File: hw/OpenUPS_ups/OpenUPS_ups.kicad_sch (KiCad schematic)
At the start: 15 parts, among them J101 XT60PW-M, J102 Barrel Jack, J103 Screw Terminal, J104 Screw Terminal, J105 Screw Terminal, J106 JST XH, J107 JST XH, U101 AVR32DB28x-xSO

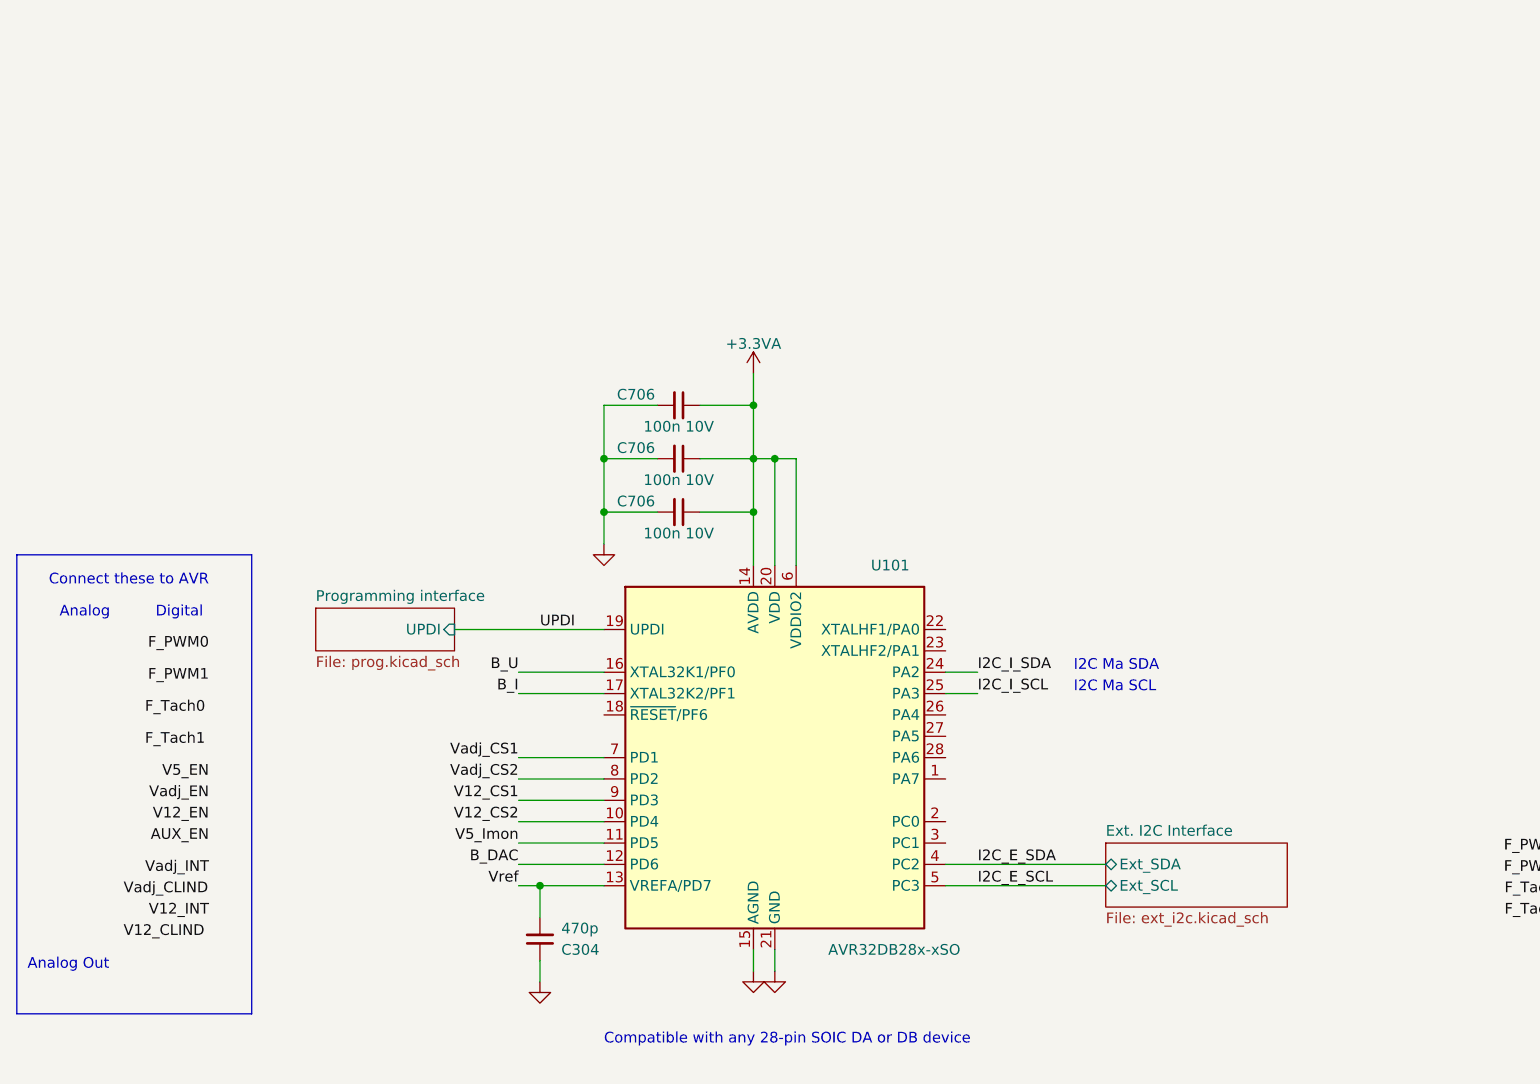
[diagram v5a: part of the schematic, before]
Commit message: Issue #20: replaced AVR with 48-pin TQFP
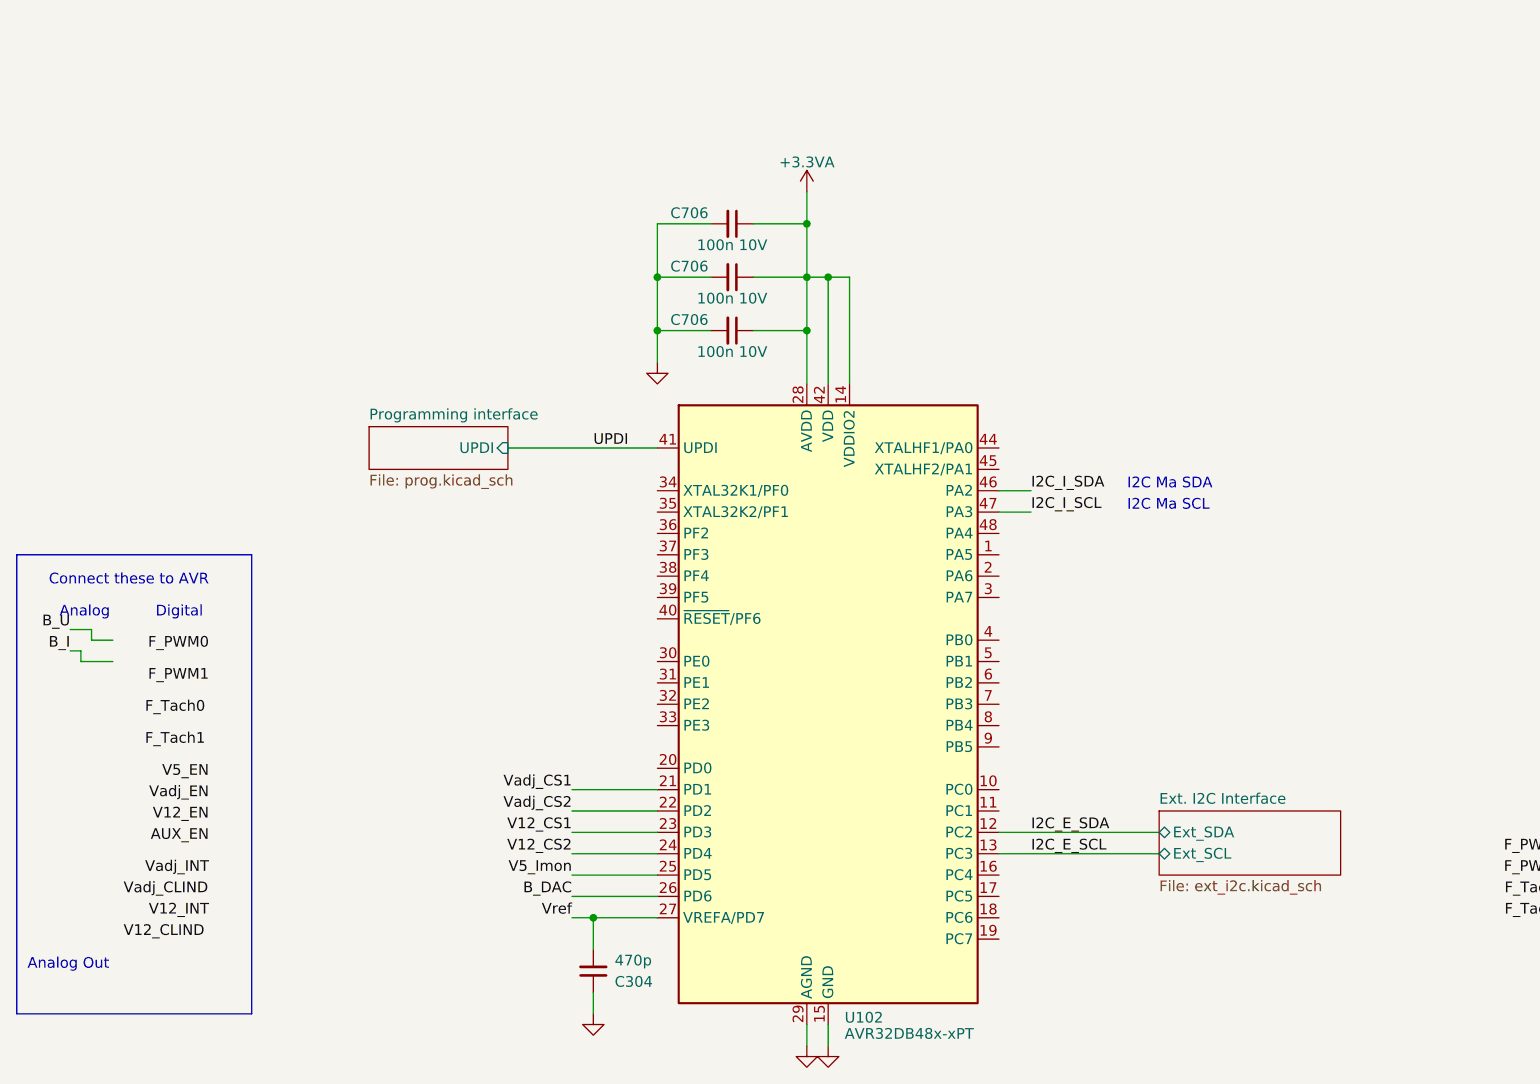
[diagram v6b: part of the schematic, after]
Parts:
- removed U101: AVR32DB28x-xSO, Package_SO:SOIC-28W_7.5x17.9mm_P1.27mm, symbol MCU_Microchip_AVR_Dx:AVR32DB28x-xSO
- added U102: AVR32DB48x-xPT, Package_QFP:TQFP-48_7x7mm_P0.5mm, symbol MCU_Microchip_AVR_Dx:AVR32DB48x-xPT
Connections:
- net +3.3VA: now also U102.14 (VDDIO2), U102.28 (AVDD), U102.42 (VDD)
- net B_DAC: now also U102.26 (PD6)
- net GND: now also U102.15 (GND), U102.29 (AGND), U102.43 (GND)
- net I2C_E_SCL: now also U102.13 (PC3)
- net I2C_E_SDA: now also U102.12 (PC2)
- net I2C_I_SCL: now also U102.47 (PA3)
- net I2C_I_SDA: now also U102.46 (PA2)
- net UPDI: now also U102.41 (UPDI)
- net V12_CS1: now also U102.23 (PD3)
- net V12_CS2: now also U102.24 (PD4)
- net V5_Imon: now also U102.25 (PD5)
- net Vadj_CS1: now also U102.21 (PD1)
- net Vadj_CS2: now also U102.22 (PD2)
- net Vref: now also U102.27 (VREFA/PD7)
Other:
- note removed: "Compatible with any 28-pin SOIC DA or DB device"
- moved on the sheet: C304, C706

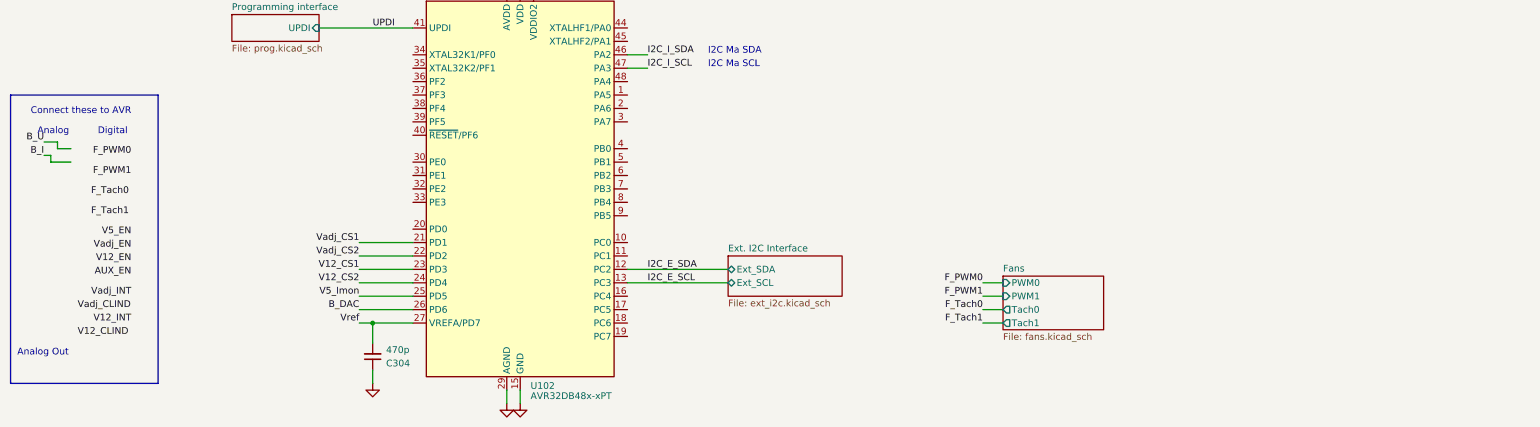
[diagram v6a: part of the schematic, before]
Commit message: Issue #16: Added LED indicators
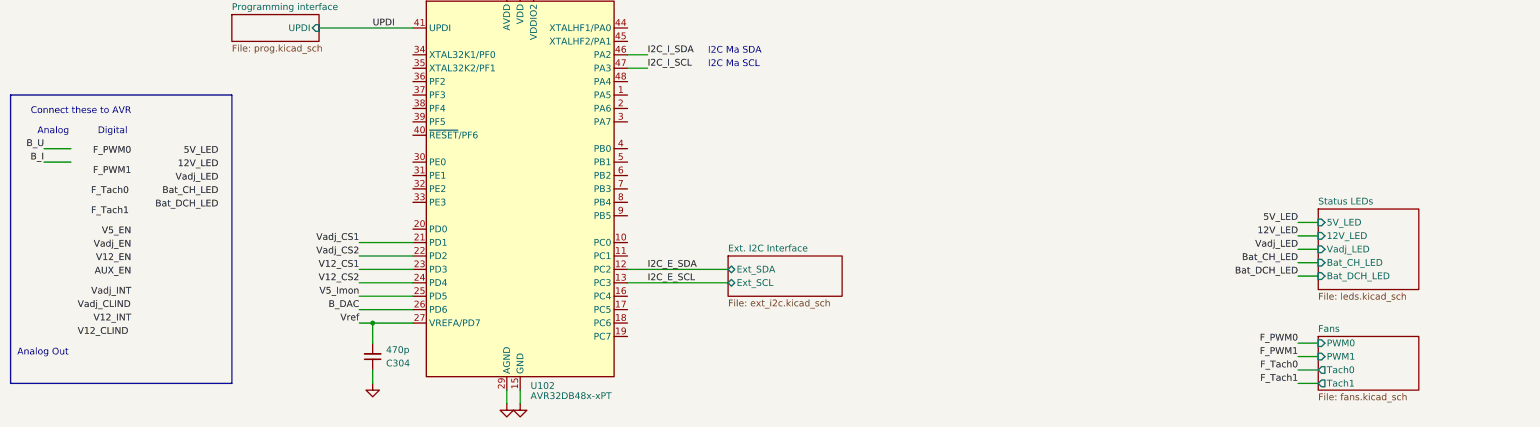
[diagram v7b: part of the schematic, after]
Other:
- added sheet Status LEDs (leds.kicad_sch)
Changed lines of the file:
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@@
+    (stroke (width 0) (type default))
+  )
+  (wire (pts (xy 265.43 241.3) (xy 269.24 241.3))
     (stroke (width 0) (type default))
   )
@@
     (stroke (width 0) (type default))
   )
+  (wire (pts (xy 265.43 248.92) (xy 269.24 248.92))
+    (stroke (width 0) (type default))
+  )
   (wire (pts (xy 90.17 261.62) (xy 90.17 257.81))
+    (stroke (width 0) (type default))
+  )
+  (wire (pts (xy 265.43 243.84) (xy 269.24 243.84))
     (stroke (width 0) (type default))
   )
@@
     (stroke (width 0.5) (type default))
   )
-  (wire (pts (xy 29.21 227.33) (xy 33.02 227.33))
+  (wire (pts (xy 27.94 227.33) (xy 33.02 227.33))
     (stroke (width 0) (type default))
   )
@@
     (stroke (width 0) (type default))
   )
-  (wire (pts (xy 205.74 252.73) (xy 209.55 252.73))
+  (wire (pts (xy 265.43 264.16) (xy 269.24 264.16))
     (stroke (width 0) (type default))
   )
@@
     (stroke (width 0) (type default))
   )
-  (wire (pts (xy 209.55 255.27) (xy 205.74 255.27))
+  (wire (pts (xy 269.24 266.7) (xy 265.43 266.7))
     (stroke (width 0) (type default))
   )
@@
     (stroke (width 0) (type default))
   )
-  (wire (pts (xy 30.48 224.79) (xy 33.02 224.79))
+  (wire (pts (xy 27.94 224.79) (xy 33.02 224.79))
     (stroke (width 0) (type default))
   )
@@
     (stroke (width 0) (type default))
   )
-  (wire (pts (xy 205.74 250.19) (xy 209.55 250.19))
-    (stroke (width 0) (type default))
-  )
-  (wire (pts (xy 29.21 226.06) (xy 29.21 227.33))
+  (wire (pts (xy 265.43 261.62) (xy 269.24 261.62))
     (stroke (width 0) (type default))
   )
@@
     (stroke (width 0) (type default))
   )
-  (wire (pts (xy 30.48 223.52) (xy 30.48 224.79))
-    (stroke (width 0) (type default))
-  )
   (wire (pts (xy 90.17 58.42) (xy 90.17 49.53))
     (stroke (width 0.5) (type default))
@@
     (stroke (width 0) (type default))
   )
-  (wire (pts (xy 209.55 257.81) (xy 205.74 257.81))
+  (wire (pts (xy 269.24 269.24) (xy 265.43 269.24))
     (stroke (width 0) (type default))
   )
@@
     (stroke (width 0) (type default))
   )
+  (wire (pts (xy 265.43 246.38) (xy 269.24 246.38))
+    (stroke (width 0) (type default))
+  )
   (wire (pts (xy 307.34 85.09) (xy 299.72 85.09))
     (stroke (width 0) (type default))
@@
     (stroke (width 0) (type default))
   )
-  (wire (pts (xy 27.94 223.52) (xy 30.48 223.52))
-    (stroke (width 0) (type default))
-  )
   (wire (pts (xy 302.26 87.63) (xy 302.26 88.9))
     (stroke (width 0) (type default))
@@
   )
   (wire (pts (xy 285.75 44.45) (xy 285.75 46.99))
-    (stroke (width 0) (type default))
-  )
-  (wire (pts (xy 27.94 226.06) (xy 29.21 226.06))
     (stroke (width 0) (type default))
   )
@@
     (stroke (width 0) (type default))
   )
+  (wire (pts (xy 265.43 238.76) (xy 269.24 238.76))
+    (stroke (width 0) (type default))
+  )
   (wire (pts (xy 50.8 68.58) (xy 54.61 68.58))
     (stroke (width 0) (type default))
@@
     (stroke (width 0) (type default))
   )
-  (rectangle (start 21.59 214.63) (end 49.53 269.24)
+  (rectangle (start 21.59 214.63) (end 63.5 269.24)
     (stroke (width 0) (type default))
     (fill (type none))
@@
     (effects (font (size 1.27 1.27)) (justify left bottom))
   )
+  (label "12V_LED" (at 60.96 228.6 180) (fields_autoplaced)
+    (effects (font (size 1.27 1.27)) (justify right bottom))
+  )
   (label "V12_CLIND" (at 34.29 260.35 0) (fields_autoplaced)
     (effects (font (size 1.27 1.27)) (justify left bottom))
   )
+  (label "Vadj_LED" (at 60.96 231.14 180) (fields_autoplaced)
+    (effects (font (size 1.27 1.27)) (justify right bottom))
+  )
   (label "Vadj_INT" (at 44.45 252.73 180) (fields_autoplaced)
     (effects (font (size 1.27 1.27)) (justify right bottom))
@@
     (effects (font (size 1.27 1.27)) (justify left bottom))
   )
+  (label "Bat_DCH_LED" (at 265.43 248.92 180) (fields_autoplaced)
+    (effects (font (size 1.27 1.27)) (justify right bottom))
+  )
   (label "V12_CLIND" (at 234.95 85.09 0) (fields_autoplaced)
     (effects (font (size 1.27 1.27)) (justify left bottom))
@@
     (effects (font (size 1.27 1.27)) (justify right bottom))
   )
+  (label "5V_LED" (at 265.43 238.76 180) (fields_autoplaced)
+    (effects (font (size 1.27 1.27)) (justify right bottom))
+  )
   (label "I2C_E_SCL" (at 142.24 250.19 0) (fields_autoplaced)
     (effects (font (size 1.27 1.27)) (justify left bottom))
@@
     (effects (font (size 1.27 1.27)) (justify right bottom))
   )
-  (label "F_Tach0" (at 205.74 255.27 180) (fields_autoplaced)
-    (effects (font (size 1.27 1.27)) (justify right bottom))
-  )
-  (label "B_U" (at 27.94 223.52 180) (fields_autoplaced)
+  (label "F_Tach0" (at 265.43 266.7 180) (fields_autoplaced)
+    (effects (font (size 1.27 1.27)) (justify right bottom))
+  )
+  (label "B_U" (at 27.94 224.79 180) (fields_autoplaced)
     (effects (font (size 1.27 1.27)) (justify right bottom))
   )
@@
     (effects (font (size 1.27 1.27)) (justify right bottom))
   )
+  (label "Bat_CH_LED" (at 265.43 246.38 180) (fields_autoplaced)
+    (effects (font (size 1.27 1.27)) (justify right bottom))
+  )
   (label "V5_EN" (at 203.2 120.65 180) (fields_autoplaced)
     (effects (font (size 1.27 1.27)) (justify right bottom))
@@
     (effects (font (size 1.27 1.27)) (justify right bottom))
   )
-  (label "F_PWM0" (at 205.74 250.19 180) (fields_autoplaced)
+  (label "5V_LED" (at 60.96 226.06 180) (fields_autoplaced)
+    (effects (font (size 1.27 1.27)) (justify right bottom))
+  )
+  (label "F_PWM0" (at 265.43 261.62 180) (fields_autoplaced)
+    (effects (font (size 1.27 1.27)) (justify right bottom))
+  )
+  (label "Bat_CH_LED" (at 60.96 233.68 180) (fields_autoplaced)
     (effects (font (size 1.27 1.27)) (justify right bottom))
   )
@@
     (effects (font (size 1.27 1.27)) (justify right bottom))
   )
-  (label "B_I" (at 27.94 226.06 180) (fields_autoplaced)
+  (label "B_I" (at 27.94 227.33 180) (fields_autoplaced)
     (effects (font (size 1.27 1.27)) (justify right bottom))
   )
@@
     (effects (font (size 1.27 1.27)) (justify right bottom))
   )
+  (label "Bat_DCH_LED" (at 60.96 236.22 180) (fields_autoplaced)
+    (effects (font (size 1.27 1.27)) (justify right bottom))
+  )
   (label "V12_INT" (at 203.2 87.63 180) (fields_autoplaced)
     (effects (font (size 1.27 1.27)) (justify right bottom))
@@
     (effects (font (size 1.27 1.27)) (justify left bottom))
   )
+  (label "12V_LED" (at 265.43 241.3 180) (fields_autoplaced)
+    (effects (font (size 1.27 1.27)) (justify right bottom))
+  )
+  (label "Vadj_LED" (at 265.43 243.84 180) (fields_autoplaced)
+    (effects (font (size 1.27 1.27)) (justify right bottom))
+  )
   (label "Vadj_CS2" (at 234.95 54.61 0) (fields_autoplaced)
     (effects (font (size 1.27 1.27)) (justify left bottom))
@@
     (effects (font (size 1.27 1.27)) (justify right bottom))
   )
-  (label "F_Tach1" (at 205.74 257.81 180) (fields_autoplaced)
+  (label "F_Tach1" (at 265.43 269.24 180) (fields_autoplaced)
     (effects (font (size 1.27 1.27)) (justify right bottom))
   )
@@
     (effects (font (size 1.27 1.27)) (justify right bottom))
   )
-  (label "F_PWM1" (at 205.74 252.73 180) (fields_autoplaced)
+  (label "F_PWM1" (at 265.43 264.16 180) (fields_autoplaced)
     (effects (font (size 1.27 1.27)) (justify right bottom))
   )
@@
     )
   )
-  (sheet (at 209.55 248.92) (size 19.05 10.16) (fields_autoplaced)
+  (sheet (at 269.24 260.35) (size 19.05 10.16) (fields_autoplaced)
     (stroke (width 0.1524) (type solid))
     (fill (color 0 0 0 0.0000))
-    (property "Sheetname" "Fans" (at 209.55 248.2084 0)
+    (property "Sheetname" "Fans" (at 269.24 259.6384 0)
       (effects (font (size 1.27 1.27)) (justify left bottom))
     )
-    (property "Sheetfile" "fans.kicad_sch" (at 209.55 259.6646 0)
+    (property "Sheetfile" "fans.kicad_sch" (at 269.24 271.0946 0)
       (effects (font (size 1.27 1.27)) (justify left top))
     )
-    (pin "PWM0" input (at 209.55 250.19 180)
-      (effects (font (size 1.27 1.27)) (justify left))
-    )
-    (pin "PWM1" input (at 209.55 252.73 180)
-      (effects (font (size 1.27 1.27)) (justify left))
-    )
-    (pin "Tach1" output (at 209.55 257.81 180)
-      (effects (font (size 1.27 1.27)) (justify left))
-    )
-    (pin "Tach0" output (at 209.55 255.27 180)
+    (pin "PWM0" input (at 269.24 261.62 180)
+      (effects (font (size 1.27 1.27)) (justify left))
+    )
+    (pin "PWM1" input (at 269.24 264.16 180)
+      (effects (font (size 1.27 1.27)) (justify left))
+    )
+    (pin "Tach1" output (at 269.24 269.24 180)
+      (effects (font (size 1.27 1.27)) (justify left))
+    )
+    (pin "Tach0" output (at 269.24 266.7 180)
       (effects (font (size 1.27 1.27)) (justify left))
     )
@@
       )
     )
+  )
+  (sheet (at 269.24 236.22) (size 19.05 15.24) (fields_autoplaced)
+    (stroke (width 0.1524) (type solid))
+    (fill (color 0 0 0 0.0000))
+    (property "Sheetname" "Status LEDs" (at 269.24 235.5084 0)
+      (effects (font (size 1.27 1.27)) (justify left bottom))
+    )
+    (property "Sheetfile" "leds.kicad_sch" (at 269.24 252.0446 0)
+      (effects (font (size 1.27 1.27)) (justify left top))
+    )
+    (pin "5V_LED" input (at 269.24 238.76 180)
+      (effects (font (size 1.27 1.27)) (justify left))
+    )
+    (pin "Bat_DCH_LED" input (at 269.24 248.92 180)
+      (effects (font (size 1.27 1.27)) (justify left))
+    )
+    (pin "12V_LED" input (at 269.24 241.3 180)
+      (effects (font (size 1.27 1.27)) (justify left))
+    )
+    (pin "Vadj_LED" input (at 269.24 243.84 180)
+      (effects (font (size 1.27 1.27)) (justify left))
+    )
+    (pin "Bat_CH_LED" input (at 269.24 246.38 180)
+      (effects (font (size 1.27 1.27)) (justify left))
+    )
+    (instances
+      (project "OpenUPS_ups"
+        (path "/f77faec3-eac4-47f3-a2de-ec4a039f4502" (page "12"))
+      )
+    )
